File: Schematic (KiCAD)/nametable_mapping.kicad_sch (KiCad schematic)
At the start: 38 parts

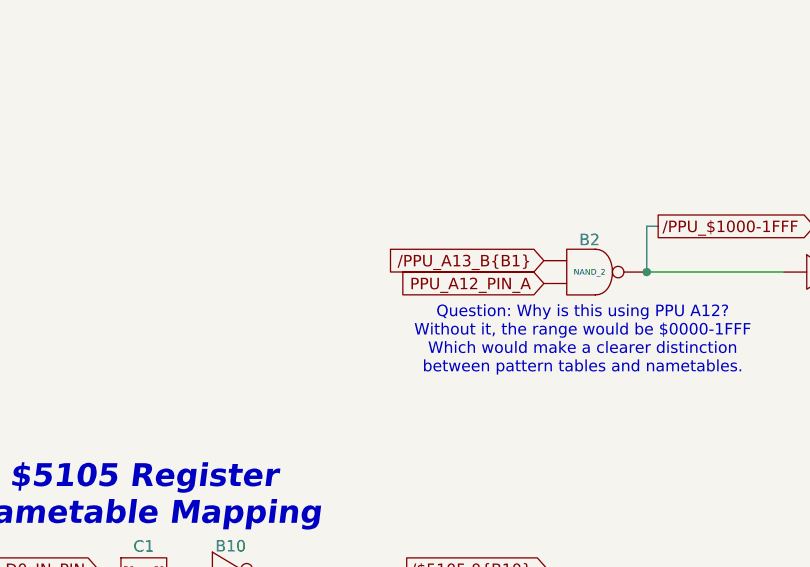
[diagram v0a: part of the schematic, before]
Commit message: - Started work on the pulse channels.  - Solved at least 2 of the red traces in the SVG.  - Finally realized that "Unknown 4to1" cells are actually just ordinary And-Or-Invert "AOI22" cells.
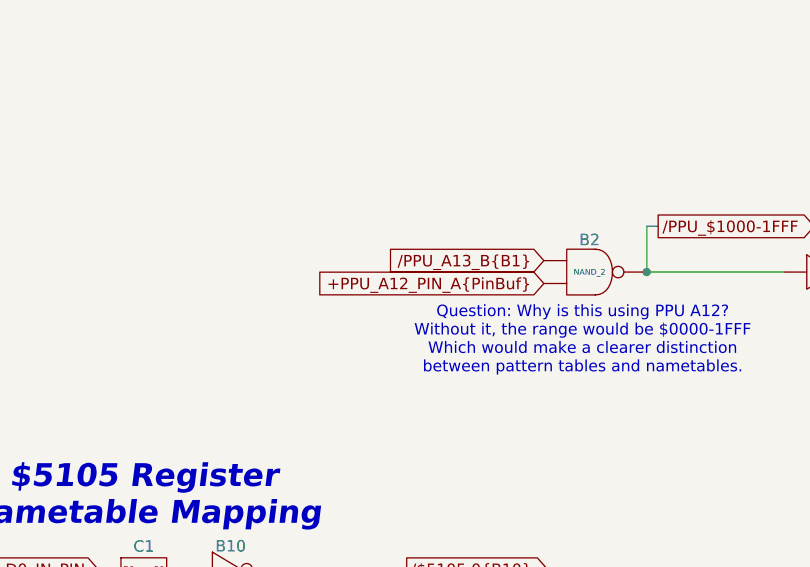
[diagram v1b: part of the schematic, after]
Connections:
- net PPU_A12_PIN_A is gone; now on net /PPU_A13_B{B1}: B2. (X)
- net at A10. (X): now also A15. (X); no longer A11. (X)
- new net: B9. (X), C1. (/Q7)
- new net: A13. (X), A14. (X), B18. (X), B19. (X), B20. (X), B21. (X), B22. (X), B23. (X), B24. (X), B25. (X)
- new net: A9. (Y4), B25. (X)
- new net: B6. (X), C1. (/Q7)
- new net: A9. (Y4), B23. (X)
- new net: A16. (X), B14. (X), B15. (X), B16. (X), B17. (X)
- new net: A13. (X), B14. (X), B15. (X), B16. (X), B17. (X)
- new net: A9. (Y4), B16. (X)
- new net: B10. (X), C1. (/Q7)
- new net: A9. (Y4), B15. (X)
- new net: B7. (X), C1. (/Q7)
- new net: A11. (X), A12. (X)
- new net: A10. (X), A11. (X)
- new net: B4. (X), C1. (/Q7)
- new net: B11. (X), C1. (/Q7)
- new net: B3. (X), C1. (/Q7)
- new net: A9. (Y4), B22. (X)
- new net: A17. (X), C1. (/Q7)
- new net: A9. (Y4), B14. (X)
- new net: A9. (Y4), B21. (X)
- new net: A9. (Y4), B18. (X)
- new net: A9. (Y4), B20. (X)
- new net: A9. (Y4), B19. (X)
- new net: A9. (Y4), B17. (X)
- new net: A9. (Y4), B24. (X)
- new net: B13. (X), C1. (/Q7)
- new net: B12. (X), C1. (/Q7)
- new net: B5. (X), C1. (/Q7)
- new net: B8. (X), C1. (/Q7)
- new net +PPU_A12_PIN_A{PinBuf}: B2. (X)
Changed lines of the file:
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@@
 		)
 	)
-	(global_label "PPU_A12_PIN_A"
+	(global_label "+PPU_A12_PIN_A{PinBuf}"
 		(shape input)
 		(at 119.38 109.22 180)
@@
 		)
 		(property "Intersheetrefs" "${INTERSHEET_REFS}"
-			(at 101.82 109.22 0)
+			(at 92.3857 109.22 0)
 			(effects
 				(font

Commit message: - Pulse DAC logic is now complete.  - The 4-bit adders are verified correct using Excel.    - This revealed 1 tracing error and also 3 XNOR gates that are actually XOR in this case.  - Now including a PDF version of the schematic.
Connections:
- net at A10. (X): now also A15. (X); no longer A11. (X)
- new net: B9. (X), C1. (/Q7)
- new net: A13. (X), A14. (X), B18. (X), B19. (X), B20. (X), B21. (X), B22. (X), B23. (X), B24. (X), B25. (X)
- new net: A9. (Y4), B25. (X)
- new net: B6. (X), C1. (/Q7)
- new net: A9. (Y4), B23. (X)
- new net: A16. (X), B14. (X), B15. (X), B16. (X), B17. (X)
- new net: A13. (X), B14. (X), B15. (X), B16. (X), B17. (X)
- new net: A9. (Y4), B16. (X)
- new net: B10. (X), C1. (/Q7)
- new net: A9. (Y4), B15. (X)
- new net: B7. (X), C1. (/Q7)
- new net: A11. (X), A12. (X)
- new net: A10. (X), A11. (X)
- new net: B4. (X), C1. (/Q7)
- new net: B11. (X), C1. (/Q7)
- new net: B3. (X), C1. (/Q7)
- new net: A9. (Y4), B22. (X)
- new net: A17. (X), C1. (/Q7)
- new net: A9. (Y4), B14. (X)
- new net: A9. (Y4), B21. (X)
- new net: A9. (Y4), B18. (X)
- new net: A9. (Y4), B20. (X)
- new net: A9. (Y4), B19. (X)
- new net: A9. (Y4), B17. (X)
- new net: A9. (Y4), B24. (X)
- new net: B13. (X), C1. (/Q7)
- new net: B12. (X), C1. (/Q7)
- new net: B5. (X), C1. (/Q7)
- new net: B8. (X), C1. (/Q7)
